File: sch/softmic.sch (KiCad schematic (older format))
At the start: 87 parts, among them J1 USB-C Connector, J3 XLR-OUT, J4 AudioJack 3.5mm, P1 4V1, P10 none, P2 4V1, P3 4V1, P4 4V1, P5 4V1, P6 VccPad, P7 none, P8 none, P9 none, Q1 MCP1812BT-033, Q10 ESP32-WROOM, Q11 BC847BS-TP, Q2 MMBFJ201, Q3 CH340G, Q4 BSS64AT116, Q5 OPA1671, Q6 OPA1671, Q7 BQ21040, Q8 MAX11613, Q9 Oled_128_32, SW1 RST, Y1 12MHz

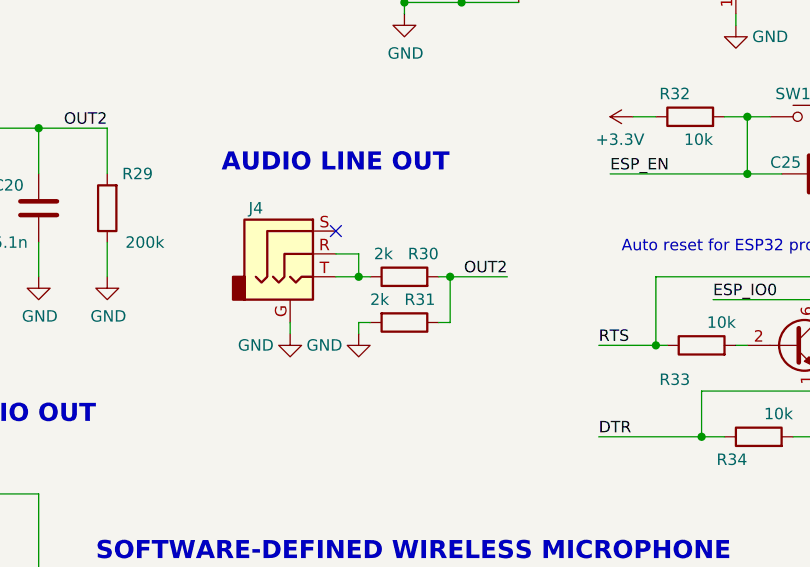
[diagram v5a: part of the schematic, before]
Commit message: added small headphone volume potentiomenter
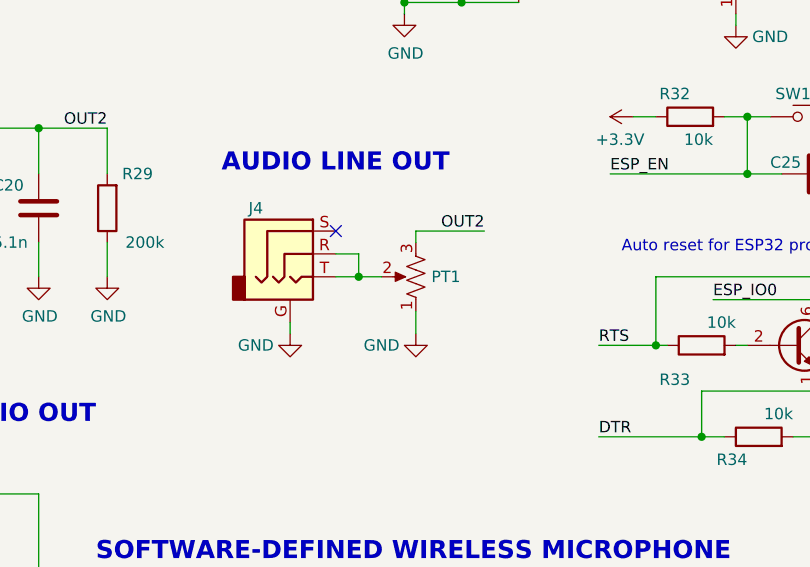
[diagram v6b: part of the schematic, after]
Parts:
- removed R30, R31: 2k, Resistor_SMD:R_0603_1608Metric, symbol Device:R
- added PT1: 200k, Potentiometer_SMD:Potentiometer_Bourns_3224W_Vertical, symbol Device:R_POT_US
- logo1: Alternative none -> (none); Description none -> Logo; Digikey none -> (none); Farnell none -> (none); Feed none -> (none); Logo - not a component none -> (none); Mouser none -> (none); mpn none -> (none)
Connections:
- wire segments 254 -> 251
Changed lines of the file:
@@
 F 2 "Symbol:OSHW-Logo2_7.3x6mm_SilkScreen" H 10700 6800 50  0001 C CNN
 F 3 "~" H 10700 6800 50  0001 C CNN
-F 4 "none" H 10700 6800 50  0001 C CNN "Description"
-F 5 "none" H 10700 6800 50  0001 C CNN "mpn"
-F 6 "none" H 10700 6800 50  0001 C CNN "Mouser"
-F 7 "none" H 10700 6800 50  0001 C CNN "Farnell"
-F 8 "none" H 10700 6800 50  0001 C CNN "Digikey"
-F 9 "none" H 10700 6800 50  0001 C CNN "Alternative"
-F 10 "none" H 10700 6800 50  0001 C CNN "Feed"
-F 11 "none" H 10700 6800 50  0001 C CNN "Logo - not a component"
+F 4 "Logo" H 10700 6800 50  0001 C CNN "Description"
 	1    10700 6800
 	1    0    0    -1
@@
 Connection ~ 8250 5600
 Wire Wire Line
-	8250 5600 8300 5600
-Text Label 8900 5600 2    50   ~ 0
+	8250 5600 8350 5600
+Text Label 8800 5400 2    50   ~ 0
 OUT2
 $Comp
-L Device:R R30
-U 1 1 5EA8B4EC
-P 8450 5600
-F 0 "R30" V 8550 5450 50  0000 L CNN
-F 1 "2k" V 8550 5650 50  0000 L CNN
-F 2 "Resistor_SMD:R_0603_1608Metric" V 8380 5600 50  0001 C CNN
-F 3 "~" H 8450 5600 50  0001 C CNN
-F 4 "none" H 8450 5600 50  0001 C CNN "Manufacturer"
-F 5 "none" H 8450 5600 50  0001 C CNN "MPN"
-F 6 "RES SMD 2K OHM 1% 1/10W 0603" H 8450 5600 50  0001 C CNN "Description"
-F 7 "311-2.00KHRCT-ND" H 8450 5600 50  0001 C CNN "Digikey PN"
-F 8 "$0.10" H 8450 5600 50  0001 C CNN "Digikey Price"
-F 9 "603-RC0603FR-072KL" H 8450 5600 50  0001 C CNN "Mouser PN"
-F 10 "$0.10" H 8450 5600 50  0001 C CNN "Mouser Price"
-F 11 "C163892" H 8450 5600 50  0001 C CNN "LCSC PN"
-F 12 "$0.001847" H 8450 5600 50  0001 C CNN "LCSC Price"
-	1    8450 5600
-	0    -1   -1   0
-$EndComp
-Wire Wire Line
-	8600 5600 8650 5600
-$Comp
-L Device:R R31
-U 1 1 5EAB823C
-P 8450 5800
-F 0 "R31" V 8350 5800 50  0000 L CNN
-F 1 "2k" V 8350 5650 50  0000 L CNN
-F 2 "Resistor_SMD:R_0603_1608Metric" V 8380 5800 50  0001 C CNN
-F 3 "~" H 8450 5800 50  0001 C CNN
-F 4 "none" H 8450 5800 50  0001 C CNN "Manufacturer"
-F 5 "none" H 8450 5800 50  0001 C CNN "MPN"
-F 6 "RES SMD 2K OHM 1% 1/10W 0603" H 8450 5800 50  0001 C CNN "Description"
-F 7 "311-2.00KHRCT-ND" H 8450 5800 50  0001 C CNN "Digikey PN"
-F 8 "$0.10" H 8450 5800 50  0001 C CNN "Digikey Price"
-F 9 "603-RC0603FR-072KL" H 8450 5800 50  0001 C CNN "Mouser PN"
-F 10 "$0.10" H 8450 5800 50  0001 C CNN "Mouser Price"
-F 11 "C163892" H 8450 5800 50  0001 C CNN "LCSC PN"
-F 12 "$0.001847" H 8450 5800 50  0001 C CNN "LCSC Price"
-	1    8450 5800
-	0    1    1    0
-$EndComp
-Wire Wire Line
-	8650 5800 8650 5600
-Connection ~ 8650 5600
-Wire Wire Line
-	8650 5600 8900 5600
-Wire Wire Line
-	8600 5800 8650 5800
-Wire Wire Line
-	8300 5800 8250 5800
-$Comp
 L power:GND #PWR046
 U 1 1 5EB092F6
-P 8250 5850
-F 0 "#PWR046" H 8250 5600 50  0001 C CNN
-F 1 "GND" H 8100 5800 50  0000 C CNN
-F 2 "" H 8250 5850 50  0001 C CNN
-F 3 "" H 8250 5850 50  0001 C CNN
-	1    8250 5850
+P 8500 5850
+F 0 "#PWR046" H 8500 5600 50  0001 C CNN
+F 1 "GND" H 8350 5800 50  0000 C CNN
+F 2 "" H 8500 5850 50  0001 C CNN
+F 3 "" H 8500 5850 50  0001 C CNN
+	1    8500 5850
 	1    0    0    -1
 $EndComp
-Wire Wire Line
-	8250 5800 8250 5850
 Text Notes 6050 -150 0    67   ~ 0
 ESP32 HARDWARE GUIDE\n\nhttps://www.espressif.com/sites/default/files/documentation/esp32_hardware_design_guidelines_en.pdf
@@
 	1    0    0    -1
 $EndComp
+$Comp
+L Device:R_POT_US PT1
+U 1 1 5EA036E0
+P 8500 5600
+F 0 "PT1" H 8432 5600 50  0000 R CNN
+F 1 "200k" H 8432 5645 50  0001 R CNN
+F 2 "Potentiometer_SMD:Potentiometer_Bourns_3224W_Vertical" H 8500 5600 50  0001 C CNN
+F 3 "https://eu.mouser.com/datasheet/2/54/pvg3-1084610.pdf" H 8500 5600 50  0001 C CNN
+F 4 "Trimmer Resistors, SMD 200KOhm 20% 1/4W" H 8500 5600 50  0001 C CNN "Description"
+F 5 "PVG3G204C01R00 " H 8500 5600 50  0001 C CNN "Digikey PN"
+F 6 "$1.57" H 8500 5600 50  0001 C CNN "Digikey Price"
+F 7 "PVG3G204C01R00 " H 8500 5600 50  0001 C CNN "MPN"
+F 8 "Bourns" H 8500 5600 50  0001 C CNN "Manufacturer"
+F 9 "81-PVG3G204C01R00 " H 8500 5600 50  0001 C CNN "Mouser PN"
+F 10 "$1.60" H 8500 5600 50  0001 C CNN "Mouser Price"
+	1    8500 5600
+	-1   0    0    1
+$EndComp
+Wire Wire Line
+	8500 5750 8500 5850
+Wire Wire Line
+	8500 5400 8800 5400
+Wire Wire Line
+	8500 5400 8500 5450
 $EndSCHEMATC

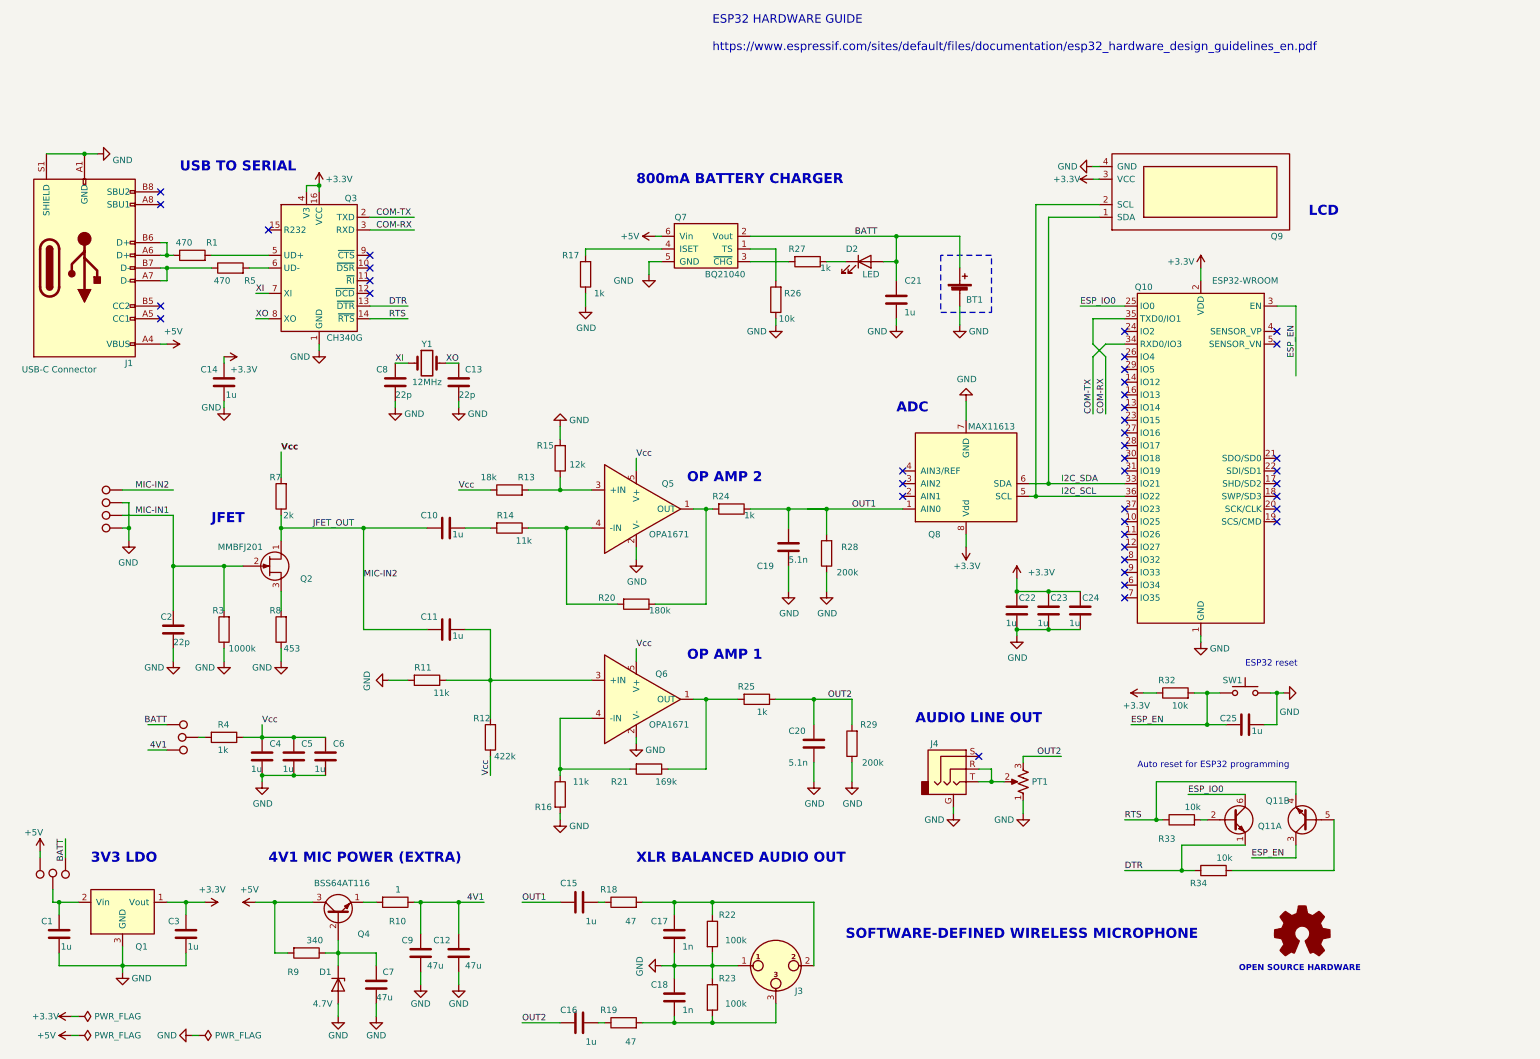
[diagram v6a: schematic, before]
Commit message: changed all resistors to 0805 case resistors
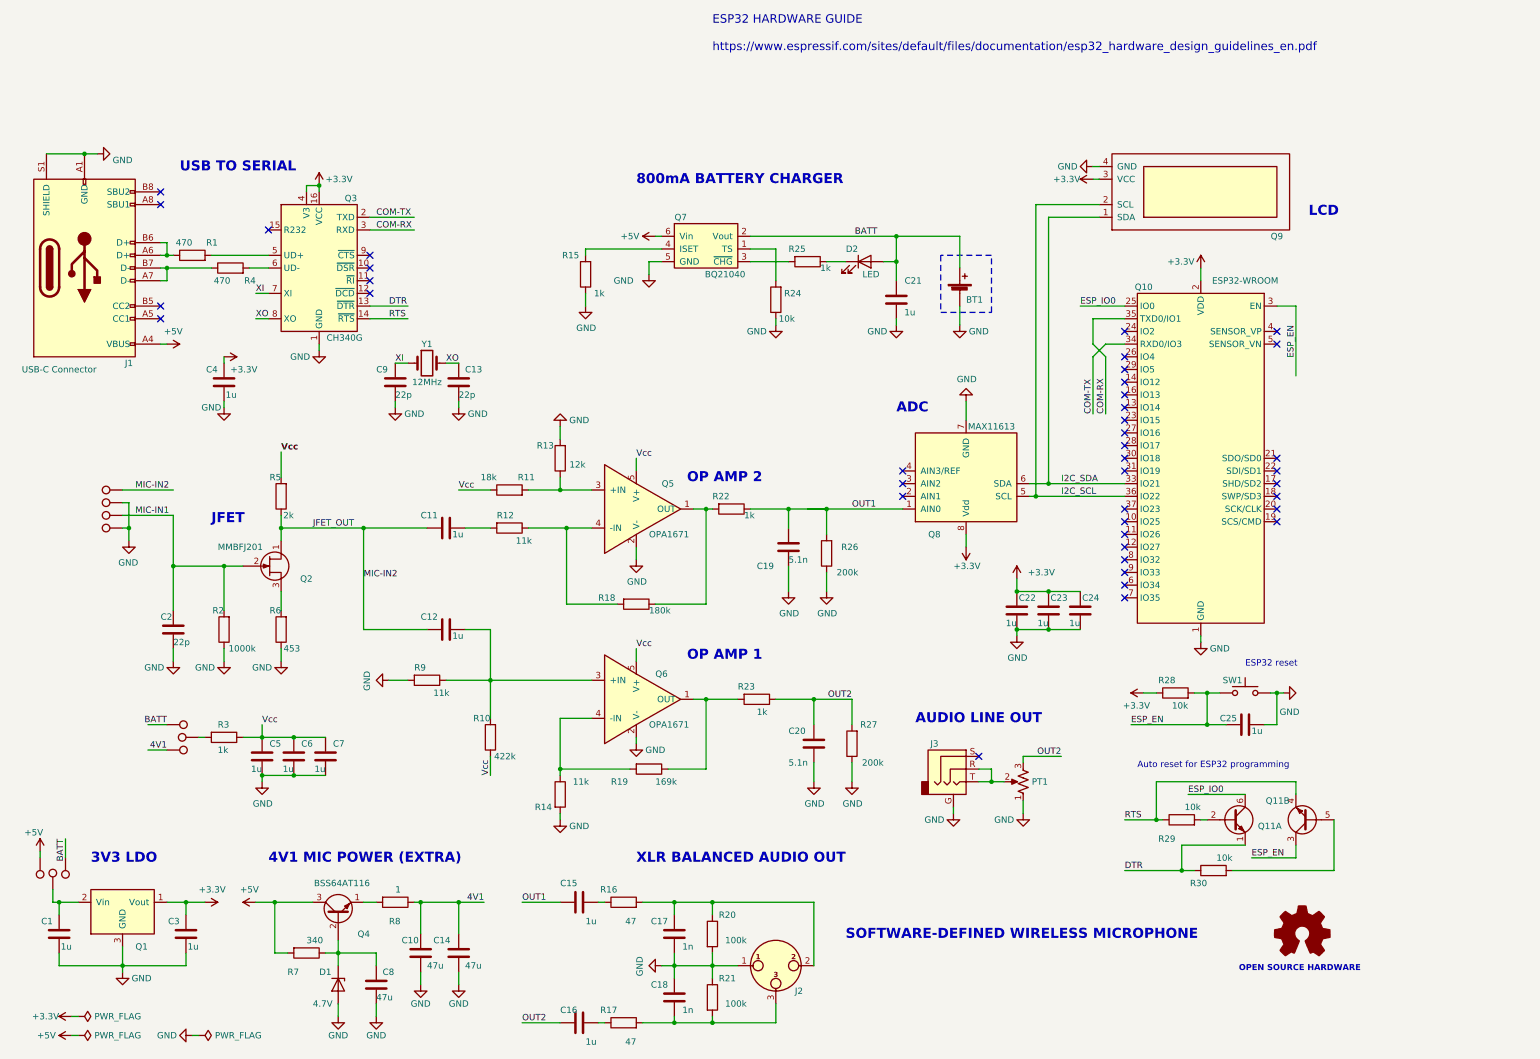
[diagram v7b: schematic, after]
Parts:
- R1: footprint Resistor_SMD:R_0603_1608Metric -> Resistor_SMD:R_0805_2012Metric_Pad1.15x1.40mm_HandSolder; Description RES SMD 470 OHM 1% 1/10W 0603 -> RES SMD 470 OHM 1% 1/10W 0805; Mouser Price none -> $0.10
- R10: renamed from R12; footprint Resistor_SMD:R_0603_1608Metric -> Resistor_SMD:R_0805_2012Metric_Pad1.15x1.40mm_HandSolder; Description RES 422K OHM 1% 1/10W 0603 -> RES 422K OHM 1% 1/10W 0805; Digikey PN 2019-RK73H1JTTD4223FCT-ND -> none; LCSC PN C23169 -> none; Mouser PN 652-CR0603FX-4223ELF -> none
- R11: renamed from R13; footprint Resistor_SMD:R_0603_1608Metric -> Resistor_SMD:R_0805_2012Metric_Pad1.15x1.40mm_HandSolder; Description RES 18k OHM 1% 1/10W 0603 -> RES 18k OHM 1% 1/10W 0805; Digikey PN A129703CT-ND -> none; LCSC PN C25810 -> none; Mouser PN 755-SFR03EZPF1802 -> none
- R12: renamed from R14; footprint Resistor_SMD:R_0603_1608Metric -> Resistor_SMD:R_0805_2012Metric_Pad1.15x1.40mm_HandSolder; Description RES 11K OHM 1% 1/8W 0603 -> RES 11K OHM 1% 1/8W 0805; Digikey PN RNCP0603FTD11K0CT-ND -> none; LCSC PN C321684 -> none; Mouser PN CRCW060311K0FKEA -> none
- R13: renamed from R15; footprint Resistor_SMD:R_0603_1608Metric -> Resistor_SMD:R_0805_2012Metric_Pad1.15x1.40mm_HandSolder; Description RES 12k OHM 1% 1/10W 0603 -> RES 12k OHM 1% 1/10W 0805; Digikey PN A129701CT-ND -> none; LCSC PN C136587 -> none; Mouser PN 652-CR0603FX-1202ELF -> none
- R14: renamed from R16; footprint Resistor_SMD:R_0603_1608Metric -> Resistor_SMD:R_0805_2012Metric_Pad1.15x1.40mm_HandSolder; Description RES 11K OHM 1% 1/8W 0603 -> RES 11K OHM 1% 1/8W 0805; Digikey PN RNCP0603FTD11K0CT-ND -> none; LCSC PN C321684 -> none; Mouser PN CRCW060311K0FKEA -> none
- R15: renamed from R17; footprint Resistor_SMD:R_0603_1608Metric -> Resistor_SMD:R_0805_2012Metric_Pad1.15x1.40mm_HandSolder; Description RES 1k OHM 1% 1/10W 0603 -> RES 1k OHM 1% 1/10W 0805; Digikey PN 311-1.00KHRCT-ND -> none; LCSC PN C126900 -> none; Mouser PN 71-CRCW06031K00FKEAC -> none
- R16: renamed from R18; footprint Resistor_SMD:R_0603_1608Metric -> Resistor_SMD:R_0805_2012Metric_Pad1.15x1.40mm_HandSolder; Description RES 47 OHM 1% 1/10W 0603 -> RES 47 OHM 1% 1/10W 0805; Digikey PN A129672CT-ND -> none; LCSC PN C103670 -> none; Mouser PN 71-CRCW060347R0FKEAC -> none
- R17: renamed from R19; footprint Resistor_SMD:R_0603_1608Metric -> Resistor_SMD:R_0805_2012Metric_Pad1.15x1.40mm_HandSolder; Description RES 47 OHM 1% 1/10W 0603 -> RES 47 OHM 1% 1/10W 0805; Digikey PN A129672CT-ND -> none; LCSC PN C103670 -> none; Mouser PN 71-CRCW060347R0FKEAC -> none
- R18: renamed from R20; footprint Resistor_SMD:R_0603_1608Metric -> Resistor_SMD:R_0805_2012Metric_Pad1.15x1.40mm_HandSolder; Description RES 180k OHM 1% 1/10W 0603 -> RES 180k OHM 1% 1/10W 0805; Digikey PN A129715CT-ND -> none; LCSC PN C123419 -> none; Mouser PN 652-CR0603FX-1803ELF -> none
- R19: renamed from R21; footprint Resistor_SMD:R_0603_1608Metric -> Resistor_SMD:R_0805_2012Metric_Pad1.15x1.40mm_HandSolder; Description RES 169k OHM 1% 1/10W 0603 -> RES 169k OHM 1% 1/10W 0805; Digikey PN RMCF0603FT169KCT-ND -> none; LCSC PN C100807 -> none; Mouser PN 667-ERJ-3EKF1693V -> none
- R2: renamed from R3; footprint Resistor_SMD:R_0603_1608Metric -> Resistor_SMD:R_0805_2012Metric_Pad1.15x1.40mm_HandSolder; Description RES SMD 1M OHM 1% 1/10W 0603 -> RES SMD 1M OHM 1% 1/10W 0805; Digikey PN 311-1.00MHRCT-ND -> none; LCSC PN C103201 -> none; Mouser PN 603-AC0603FR-071M1L -> none
- R20: renamed from R22; footprint Resistor_SMD:R_0603_1608Metric -> Resistor_SMD:R_0805_2012Metric_Pad1.15x1.40mm_HandSolder; Description RES 100K OHM 1% 1/10W 0603 -> RES 100K OHM 1% 1/10W 0805; Digikey PN RMCF0603FT100KCT-ND -> none; LCSC PN C269699 -> none; Mouser PN 667-ERJ-1GNF1003C -> none
- R21: renamed from R23; footprint Resistor_SMD:R_0603_1608Metric -> Resistor_SMD:R_0805_2012Metric_Pad1.15x1.40mm_HandSolder; Description RES 100K OHM 1% 1/10W 0603 -> RES 100K OHM 1% 1/10W 0805; Digikey PN RMCF0603FT100KCT-ND -> none; LCSC PN C269699 -> none; Mouser PN 667-ERJ-1GNF1003C -> none
- R22: renamed from R24; footprint Resistor_SMD:R_0603_1608Metric -> Resistor_SMD:R_0805_2012Metric_Pad1.15x1.40mm_HandSolder; Description RES 1k OHM 1% 1/10W 0603 -> RES 1k OHM 1% 1/10W 0805; Digikey PN 311-1.00KHRCT-ND -> none; LCSC PN C126900 -> none; Mouser PN 71-CRCW06031K00FKEAC -> none
- R23: renamed from R25; footprint Resistor_SMD:R_0603_1608Metric -> Resistor_SMD:R_0805_2012Metric_Pad1.15x1.40mm_HandSolder; Description RES 1k OHM 1% 1/10W 0603 -> RES 1k OHM 1% 1/10W 0805; Digikey PN 311-1.00KHRCT-ND -> none; LCSC PN C126900 -> none; Mouser PN 71-CRCW06031K00FKEAC -> none
- R24: renamed from R26; footprint Resistor_SMD:R_0603_1608Metric -> Resistor_SMD:R_0805_2012Metric_Pad1.15x1.40mm_HandSolder; Description RES SMD 10K OHM 1% 1/10W 0603 -> RES SMD 10K OHM 1% 1/10W 0805; Digikey PN 311-10.0KHRCT-ND -> none; Mouser PN 603-RC0603FR-0710KL -> none
- R25: renamed from R27; footprint Resistor_SMD:R_0603_1608Metric -> Resistor_SMD:R_0805_2012Metric_Pad1.15x1.40mm_HandSolder; Description RES 1k OHM 1% 1/10W 0603 -> RES 1k OHM 1% 1/10W 0805; Digikey PN 311-1.00KHRCT-ND -> none; LCSC PN C126900 -> none; Mouser PN 71-CRCW06031K00FKEAC -> none
- R26: renamed from R28; footprint Resistor_SMD:R_0603_1608Metric -> Resistor_SMD:R_0805_2012Metric_Pad1.15x1.40mm_HandSolder; Description RES 200k OHM 1% 1/10W 0603 -> RES 200k OHM 1% 1/10W 0805; Digikey PN 311-200KHRCT-ND -> none; LCSC PN C95331 -> none; Mouser PN 603-RC0603FR-10200KL -> none
- R27: renamed from R29; footprint Resistor_SMD:R_0603_1608Metric -> Resistor_SMD:R_0805_2012Metric_Pad1.15x1.40mm_HandSolder; Description RES 200k OHM 1% 1/10W 0603 -> RES 200k OHM 1% 1/10W 0805; Digikey PN 311-200KHRCT-ND -> none; LCSC PN C95331 -> none; Mouser PN 603-RC0603FR-10200KL -> none
- R28: renamed from R32; footprint Resistor_SMD:R_0603_1608Metric -> Resistor_SMD:R_0805_2012Metric_Pad1.15x1.40mm_HandSolder; Description RES SMD 10K OHM 1% 1/10W 0603 -> RES SMD 10K OHM 1% 1/10W 0805; Digikey PN 311-10.0KHRCT-ND -> none; Mouser PN 603-RC0603FR-0710KL -> none
- R29: renamed from R33; footprint Resistor_SMD:R_0603_1608Metric -> Resistor_SMD:R_0805_2012Metric_Pad1.15x1.40mm_HandSolder; Description RES SMD 10K OHM 1% 1/10W 0603 -> RES SMD 10K OHM 1% 1/10W 0805; Digikey PN 311-10.0KHRCT-ND -> none; Mouser PN 603-RC0603FR-0710KL -> none
- R3: renamed from R4; footprint Resistor_SMD:R_0603_1608Metric -> Resistor_SMD:R_0805_2012Metric_Pad1.15x1.40mm_HandSolder; Description RES 1k OHM 1% 1/10W 0603 -> RES 1k OHM 1% 1/10W 0805; Digikey PN 311-1.00KHRCT-ND -> none; LCSC PN C126900 -> none; Mouser PN 71-CRCW06031K00FKEAC -> none
- R30: renamed from R34; footprint Resistor_SMD:R_0603_1608Metric -> Resistor_SMD:R_0805_2012Metric_Pad1.15x1.40mm_HandSolder; Description RES SMD 10K OHM 1% 1/10W 0603 -> RES SMD 10K OHM 1% 1/10W 0805; Digikey PN 311-10.0KHRCT-ND -> none; Mouser PN 603-RC0603FR-0710KL -> none
- R4: renamed from R5; footprint Resistor_SMD:R_0603_1608Metric -> Resistor_SMD:R_0805_2012Metric_Pad1.15x1.40mm_HandSolder; Description RES SMD 470 OHM 1% 1/10W 0603 -> RES SMD 470 OHM 1% 1/10W 0805; Mouser Price none -> $0.10
- R5: renamed from R7; footprint Resistor_SMD:R_0603_1608Metric -> Resistor_SMD:R_0805_2012Metric_Pad1.15x1.40mm_HandSolder; Description RES SMD 2K OHM 1% 1/10W 0603 -> RES SMD 2K OHM 1% 1/10W 0805; Digikey PN 311-2.00KHRCT-ND -> none; LCSC PN C163892 -> none; Mouser PN 603-RC0603FR-072KL -> none
- R6: renamed from R8; footprint Resistor_SMD:R_0603_1608Metric -> Resistor_SMD:R_0805_2012Metric_Pad1.15x1.40mm_HandSolder; Description RES SMD 453 OHM 1% 1/10W 0603 -> RES SMD 453 OHM 1% 1/10W 0805; Digikey PN 311-453HRCT-ND -> none; LCSC PN C103201 -> none; Mouser PN 603-RC0603FR-07453RL -> none
- R7: renamed from R9; footprint Resistor_SMD:R_0603_1608Metric -> Resistor_SMD:R_0805_2012Metric_Pad1.15x1.40mm_HandSolder; Description RES SMD 340 OHM 0.1% 1/10W 0603 -> RES SMD 340 OHM 0.1% 1/10W 0805; Digikey PN P340DBCT-ND -> none; LCSC PN C400666 -> none; Mouser PN 652-CR0603-FX3400ELF -> none
- R8: renamed from R10; footprint Resistor_SMD:R_0603_1608Metric -> Resistor_SMD:R_0805_2012Metric_Pad1.15x1.40mm_HandSolder; Description RES SMD 1Ohm 1% 0603 -> RES SMD 1Ohm 1% 0805; Digikey PN 311-1.00HRCT-ND -> none; LCSC PN C497141 -> none; Mouser PN 71-CRCW0603J-1-E3 -> none
- R9: renamed from R11; footprint Resistor_SMD:R_0603_1608Metric -> Resistor_SMD:R_0805_2012Metric_Pad1.15x1.40mm_HandSolder; Description RES 11K OHM 1% 1/8W 0603 -> RES 11K OHM 1% 1/8W 0805; Digikey PN RNCP0603FTD11K0CT-ND -> none; LCSC PN C321684 -> none; Mouser PN CRCW060311K0FKEA -> none
- renumbered C9 to C10, C10 to C11, C11 to C12, C12 to C14, C14 to C4, C4 to C5, C5 to C6, C6 to C7, C7 to C8, C8 to C9, J3 to J2, J4 to J3, P6 to P10, P7 to P4, P8 to P5, P9 to P6, P10 to P7, P4 to P8, P5 to P9

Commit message: change all caps to 0805 case caps
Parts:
- BT1: Digikey PN (none) -> none; Digikey Price (none) -> none; LCSC PN (none) -> none; LCSC Price (none) -> none; MPN (none) -> none; Manufacturer (none) -> none; Mouser PN (none) -> none; Mouser Price (none) -> none
- C1, C11, C12, C21, C22, C23, C24, C25, C3, C4, C5, C6, C7: footprint Capacitor_SMD:C_0603_1608Metric -> Capacitor_SMD:C_0805_2012Metric_Pad1.15x1.40mm_HandSolder; Description CAP CER 1UF 10V X7R 0603 -> CAP CER 1uF 10V X7R 0805; Digikey PN 311-3484-1-ND -> none; Digikey Price $0.24 -> none; LCSC PN C458912 -> none; LCSC Price $0.023475 -> none; Mouser PN 581-0603YC105JAT2A -> none; Mouser Price $0.24 -> none
- C10, C14, C8: footprint Capacitor_SMD:C_0603_1608Metric -> Capacitor_SMD:C_0805_2012Metric_Pad1.15x1.40mm_HandSolder; Description CAP CER 47UF 2.5V X6S 0603 -> CAP CER 47uF 10V 0805; Digikey PN 490-13244-1-ND -> none; Digikey Price $0.55 -> none; LCSC PN C140782 -> none; LCSC Price $0.13 -> none; Mouser PN 963-JMK107BBJ476MARE -> none; Mouser Price $0.74 -> none
- C13, C9: footprint Capacitor_SMD:C_0603_1608Metric -> Capacitor_SMD:C_0805_2012Metric_Pad1.15x1.40mm_HandSolder; Description CAP CER 22PF 100V X7R 0603 -> CAP CER 22pF 10V X7R 0805; Digikey PN (none) -> none; Digikey Price (none) -> none; LCSC PN (none) -> none; LCSC Price (none) -> none
- C15, C16: footprint Capacitor_SMD:C_0603_1608Metric -> Capacitor_SMD:C_0805_2012Metric_Pad1.15x1.40mm_HandSolder; Description CAP CER 1UF 10V X7R 0603 -> CAP CER 1uF 100V X7R 0805; Digikey PN 311-3484-1-ND -> none; Digikey Price $0.24 -> none; LCSC PN C458912 -> none; LCSC Price $0.023475 -> none; Mouser PN 581-0603YC105JAT2A -> none; Mouser Price $0.24 -> none
- C17, C18: footprint Capacitor_SMD:C_0603_1608Metric -> Capacitor_SMD:C_0805_2012Metric_Pad1.15x1.40mm_HandSolder; Description CAP CER 1000PF 25V C0G/NP0 0603 -> CAP CER 1nF 100V X7R 0805; Digikey PN 399-7830-1-ND -> none; Digikey Price $0.10 -> none; LCSC PN C376765 -> none; LCSC Price $0.008458 -> none; Mouser PN 80-C0603C102J5RAUTO -> none; Mouser Price $0.10 -> none
- C19, C20: footprint Capacitor_SMD:C_0603_1608Metric -> Capacitor_SMD:C_0805_2012Metric_Pad1.15x1.40mm_HandSolder; Description CAP CER 5100PF 100V X7R 0603 -> CAP CER 5.1nF 10V X7R 0805; Digikey PN 478-10226-1-ND -> none; Digikey Price $0.30 -> none; LCSC PN C1587 -> none; LCSC Price $0.006256 -> none; Mouser PN 581-06031C512JAT2A -> none; Mouser Price $0.27 -> none
- C2: footprint Capacitor_SMD:C_0603_1608Metric -> Capacitor_SMD:C_0805_2012Metric_Pad1.15x1.40mm_HandSolder; Description CAP CER 22PF 100V C0G/NP0 0603 -> CAP CER 22pF 10V X7R 0805; Digikey PN 399-7874-1-ND -> none; Digikey Price $0.10 -> none; LCSC PN C107451 -> none; LCSC Price $0.007318 -> none
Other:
- note added: "There are 50V here"
